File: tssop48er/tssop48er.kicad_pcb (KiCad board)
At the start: 2 copper layers, 50 x 50 mm, 32 parts, among them P1 USB_B, U1 93CxxA, U2 AP1117, U3 FT2232, U4 TSSOP48_NAND, Y1 Crystal_Small

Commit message: misssing files
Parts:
- moved P1 1.05 mm to (160.5, 107.0)
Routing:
- net Net-(C2-Pad1): track 13.0 -> 11.3 mm
- net Net-(P1-Pad3): track 7.44 -> 9.10 mm
- net Net-(P1-Pad2): track 13.8 -> 14.8 mm
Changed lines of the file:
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@@
     (links 100)
     (no_connects 0)
-    (area 0 0 0 0)
+    (area 153.6 73 220.600001 131.300001)
     (thickness 1.6)
     (drawings 9)
-    (tracks 405)
+    (tracks 409)
     (zones 0)
     (modules 32)
@@
   (layers
     (0 F.Cu signal)
-    (31 B.Cu signal)
+    (31 B.Cu signal hide)
     (32 B.Adhes user)
     (33 F.Adhes user)
@@
     (visible_elements FFFFFF7F)
     (pcbplotparams
-      (layerselection 0x00030_80000001)
+      (layerselection 0x010f0_80000001)
       (usegerberextensions false)
       (excludeedgelayer true)
@@
       (outputformat 1)
       (mirror false)
-      (drillshape 1)
+      (drillshape 0)
       (scaleselection 1)
-      (outputdirectory ""))
+      (outputdirectory gerbers/))
   )
   (net 0 "")
@@
   )
   (module usbAtaobao:USB_A (layer F.Cu)
-    (at 161.544 106.934 90)
+    (at 160.5 107 90)
     (descr "USB A connector")
     (tags "USB USB_A")
@@
   (segment (start 169.6 104.2) (end 168.4 105.4) (width 0.25) (layer F.Cu) (net 2))
   (segment (start 168.95 104.85) (end 169.1 104.85) (width 0.25) (layer B.Cu) (net 2))
-  (segment (start 165.744 106.884) (end 165.784 106.884) (width 0.25) (layer F.Cu) (net 3))
-  (segment (start 165.784 106.884) (end 167.2 108.3) (width 0.4) (layer F.Cu) (net 3))
-  (segment (start 164.404 112.896) (end 164.404 115.578) (width 0.4) (layer F.Cu) (net 3))
-  (segment (start 167.2 110.1) (end 164.404 112.896) (width 0.4) (layer F.Cu) (net 3))
-  (segment (start 167.2 108.3) (end 167.2 110.1) (width 0.4) (layer F.Cu) (net 3))
+  (segment (start 164.404 115.578) (end 164.404 112.596) (width 0.3) (layer F.Cu) (net 3) (status 400000))
+  (segment (start 164.7 112.3) (end 164.7 106.95) (width 0.3) (layer F.Cu) (net 3) (status 800000))
+  (segment (start 164.404 112.596) (end 164.7 112.3) (width 0.3) (layer F.Cu) (net 3))
+  (segment (start 164.7 106.95) (end 164.74 106.95) (width 0.25) (layer F.Cu) (net 3) (status 30))
   (segment (start 161.864 115.598) (end 164.384 115.598) (width 0.4) (layer F.Cu) (net 3))
   (segment (start 164.384 115.598) (end 164.404 115.578) (width 0.25) (layer F.Cu) (net 3))
@@
   (via (at 172.8 99.4) (size 0.6) (drill 0.4) (layers F.Cu B.Cu) (net 10))
   (segment (start 172.8 99.4) (end 170.6 99.4) (width 0.25) (layer F.Cu) (net 10))
-  (segment (start 165.744 102.384) (end 165.744 102.056) (width 0.25) (layer F.Cu) (net 11))
-  (segment (start 165.744 102.056) (end 167.1 100.7) (width 0.25) (layer F.Cu) (net 11))
-  (segment (start 167.1 100.7) (end 167.1 99.3) (width 0.25) (layer F.Cu) (net 11))
+  (segment (start 164.7 102.45) (end 165.55 102.45) (width 0.25) (layer F.Cu) (net 11) (status 400000))
+  (segment (start 167 100.5) (end 167.1 100.5) (width 0.25) (layer F.Cu) (net 11))
+  (segment (start 167.1 100.6) (end 167 100.5) (width 0.25) (layer F.Cu) (net 11))
+  (segment (start 167.1 100.9) (end 167.1 100.6) (width 0.25) (layer F.Cu) (net 11))
+  (segment (start 165.55 102.45) (end 167.1 100.9) (width 0.25) (layer F.Cu) (net 11))
+  (segment (start 164.7 102.45) (end 164.7 102.122) (width 0.25) (layer F.Cu) (net 11) (status 30))
+  (segment (start 167.1 100.7) (end 167.1 100.5) (width 0.25) (layer F.Cu) (net 11))
+  (segment (start 167.1 100.5) (end 167.1 99.3) (width 0.25) (layer F.Cu) (net 11))
+  (segment (start 167.8 98.6) (end 170.6 98.6) (width 0.25) (layer F.Cu) (net 11))
   (segment (start 167.1 99.3) (end 167.8 98.6) (width 0.25) (layer F.Cu) (net 11))
-  (segment (start 167.8 98.6) (end 170.6 98.6) (width 0.25) (layer F.Cu) (net 11))
-  (segment (start 165.744 104.394) (end 167.006 104.394) (width 0.25) (layer F.Cu) (net 12))
+  (segment (start 164.7 104.46) (end 167.006 104.394) (width 0.25) (layer F.Cu) (net 12) (status 10))
   (segment (start 172.2 97.8) (end 170.6 97.8) (width 0.25) (layer F.Cu) (net 12))
   (segment (start 172.3 97.9) (end 172.2 97.8) (width 0.25) (layer F.Cu) (net 12))

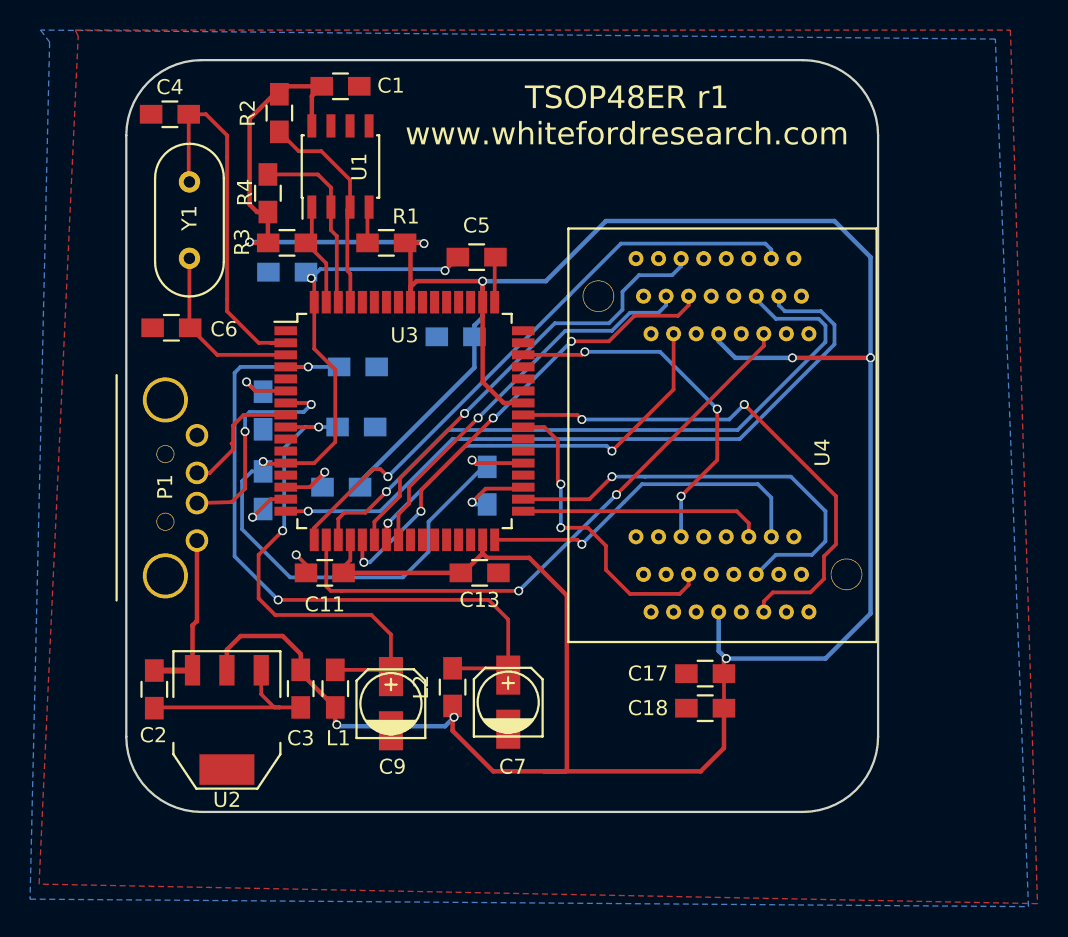
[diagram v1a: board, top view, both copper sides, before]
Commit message: updated tsop48er to r2 (changed zif socket)
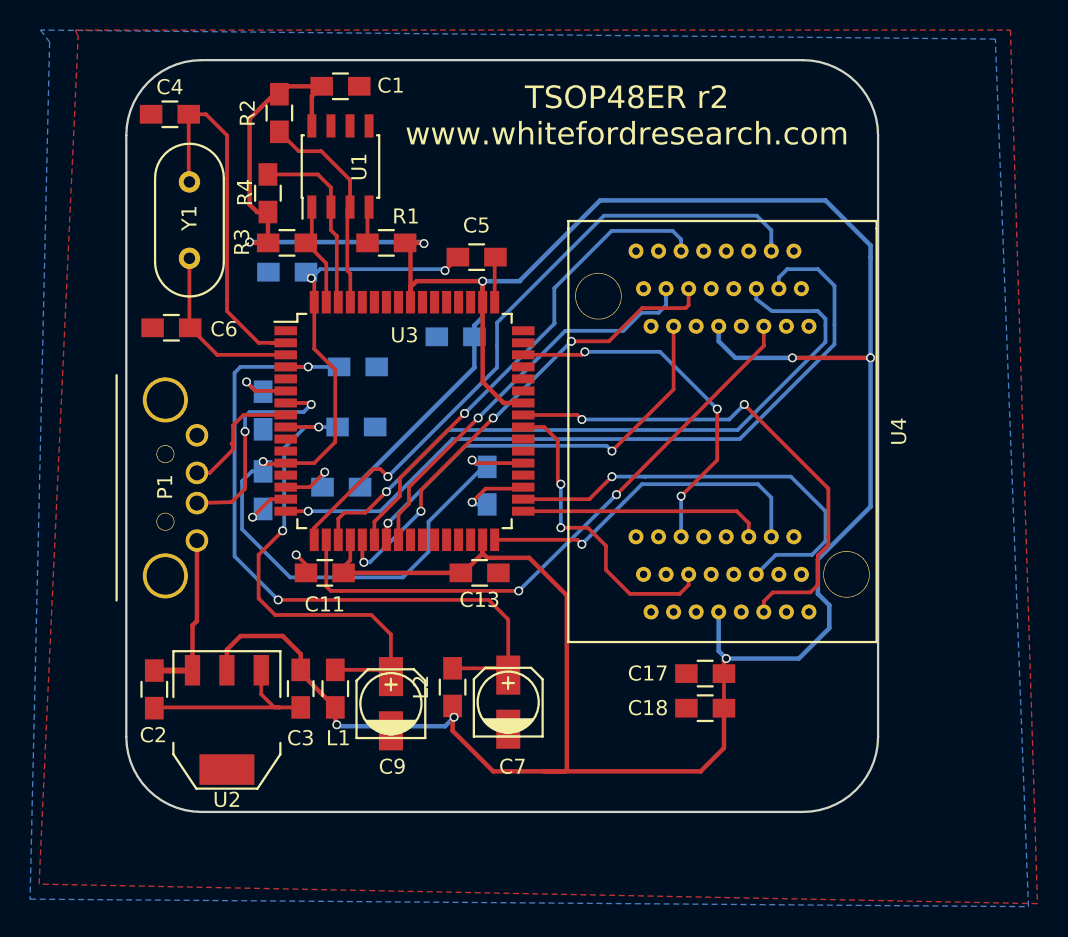
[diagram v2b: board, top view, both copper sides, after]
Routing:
- net Net-(U3-Pad17): track 40.3 -> 44.4 mm
- net Net-(U3-Pad16): track 47.2 -> 50.1 mm
- net Net-(U3-Pad22): track 30.5 -> 32.8 mm
- net +3V3: track 229.9 -> 231.1 mm
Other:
- board text added: "TSOP48ER r2 www.whitefordresearch.com"
- board text removed: "TSOP48ER r1 www.whitefordresearch.com"
